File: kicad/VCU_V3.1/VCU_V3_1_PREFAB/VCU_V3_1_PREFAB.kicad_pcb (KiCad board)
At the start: 2 copper layers, 114 x 95 mm, 145 parts, among them J1 AVR-ISP-6, J2 Conn_01x24, J3 Conn_01x24, J4 Conn_01x04_Pin, J5 USB_C_Receptacle_USB2.0_14P, Q1 MMBT3906, Q2 Q_NMOS_GDS, Q3 MMBT3906, Q4 Q_NMOS_GDS, Q5 MMBT3906, Q6 Q_NMOS_GDS, Q7 MMBT3906, Q8 Q_NMOS_GDS, SW1 SW_Push, U1 ATmega328P-A, U10 TJA1051T, U11 ADuM1201AR, U12 MCP2515-xST, U13 MCP2515-xST, U14 MCP2515-xST, U16 LTV-817S, U17 ADuM1201AR, U18 ADuM1201AR, U19 OP07, U2 LM2575-5.0BU, U20 OP07, U21 OP07, U22 OP07, U23 LTV-817S, U24 LTV-817S, U25 LTV-817S, U3 CH340N, U5 TJA1051T, U6 AMS1117-3.3, U9 TJA1051T, Y1 16MHz, Y2 20MHz, Y3 20MHz, Y4 20MHz

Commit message: VCU v3.1 changes
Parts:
- removed ? (x4): , 
- added JP1: Jumper_2_Open, Jumper:SolderJumper-2_P1.3mm_Open_Pad1.0x1.5mm, F.Cu at (214.0, 75.3)
- C34, C35, C36, C37, R40, R5: moved to F.Cu
- Q2, Q4, Q6, Q8: footprint Better_Handsolder:TO-252-2 -> RMC_TO:TO-252-2
- R33: value 1k -> 500R
- R43, R44, R45, R46: moved to B.Cu
- U10, U11, U17, U18, U5, U9: footprint Package_SO:SOIC-8_3.9x4.9mm_P1.27mm -> RMC_SO:SOIC-8_3.9x4.9mm_P1.27mm_RMC_Handsolder
- U12, U13, U14: footprint Package_SO:TSSOP-20_4.4x6.5mm_P0.65mm -> RMC_SO:TSSOP-20_4.4x6.5mm_P0.65mm
- U19, U20, U21, U22: footprint Package_SO:SOIC-8-1EP_3.9x4.9mm_P1.27mm_EP2.29x3mm -> RMC_SO:SOIC-8_3.9x4.9mm_P1.27mm_RMC_Handsolder
- U3: footprint Package_SO:SOP-8_3.9x4.9mm_P1.27mm -> RMC_SO:SOIC-8_3.9x4.9mm_P1.27mm_RMC_Handsolder
- U6: footprint Package_TO_SOT_SMD:SOT-223-3_TabPin2 -> RMC_SOT:SOT-223-3_TabPin2_Handsolder
- moved C19 19.7 mm to (205.7, 114.3)
- moved R41 14.0 mm to (113.8, 111.0), turned to 180 degrees
- moved C36 7.88 mm to (153.8, 111.6), turned to -90 degrees
- moved C35 7.07 mm to (170.4, 116.8)
- moved R44 6.66 mm to (108.5, 117.3), turned to 180 degrees
- moved C34 6.24 mm to (170.4, 111.8), turned to -90 degrees
- moved R15 5.27 mm to (184.1, 127.0), turned to 180 degrees
- moved R45 5.01 mm to (108.7, 114.0), turned to 180 degrees
- moved R40 3.76 mm to (113.8, 108.8), turned to 0 degrees
- moved C37 3.28 mm to (153.8, 117.2)
- moved U5 3.07 mm to (184.1, 119.3)
- moved U9 3.04 mm to (166.2, 119.3)
- moved U10 2.75 mm to (149.9, 119.3)
- moved D2 2.15 mm to (109.9, 96.0)
- moved C20 2.11 mm to (112.9, 101.7)
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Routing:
- net +5V: track 552.8 -> 413.0 mm, vias 21 -> 20
- net CAN3-: track 125.0 -> 9.10 mm
- net CAN3+: track 123.5 -> 9.16 mm
- net CAN+: track 102.2 -> 9.16 mm
- net CAN-: track 98.3 -> 9.10 mm
- net CAN2+: track 92.6 -> 8.29 mm
- net CAN2-: track 85.8 -> 9.10 mm
- net +12V: track 176.5 -> 212.4 mm
- net APPS_3V3_GAINED: track 79.5 -> 92.6 mm
- net APPS_5V: track 112.9 -> 99.8 mm
- net Net-(R40-Pad1): track 9.45 -> 2.31 mm, vias 1 -> 0
- net +3V3: track 45.5 -> 38.4 mm
- net INPUT_BRAKE_IN: track 23.8 -> 30.7 mm
- net Net-(U11-VIA): track 6.74 -> 0.00 mm, vias 1 -> 0
- net RXD: track 87.9 -> 94.5 mm
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
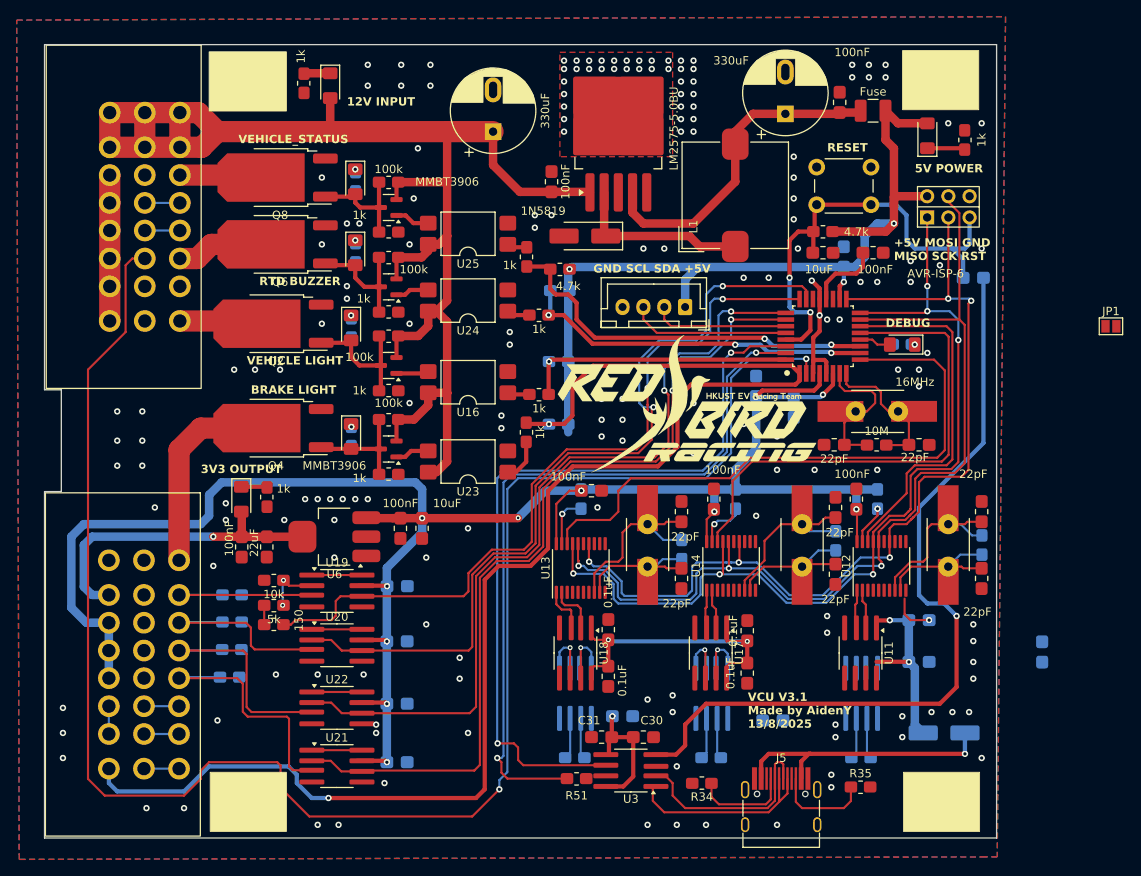
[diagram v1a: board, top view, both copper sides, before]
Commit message: VCU V3.1 preview patch v2
DRC debug
Change to pmos
remove usb c and add xh
remap pinout
rewiring
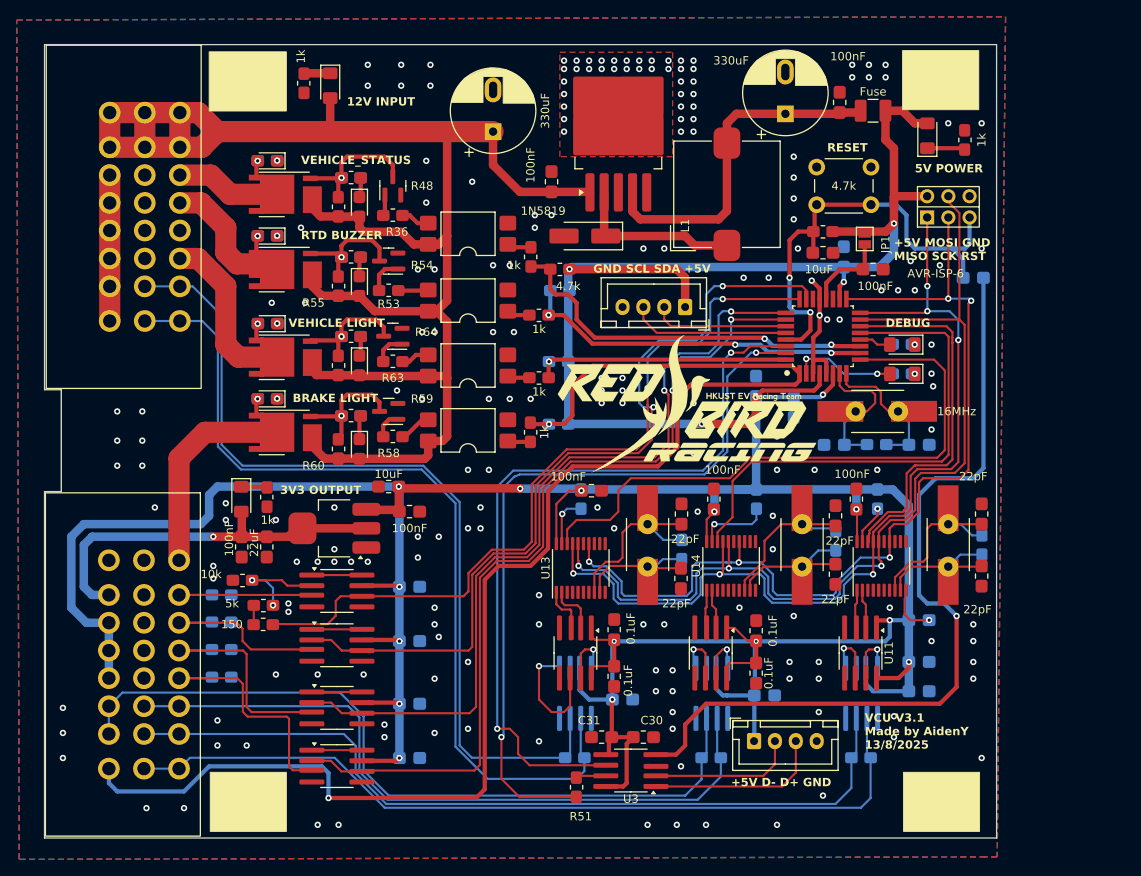
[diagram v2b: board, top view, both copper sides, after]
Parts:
- removed D4, D5, D6, D9: IR204A, LED_SMD:LED_1206_3216Metric_Pad1.42x1.75mm_HandSolder
- removed D7: D, Diode_SMD:D_SMA_Handsoldering
- removed J5: USB_C_Receptacle_USB2.0_14P, RMC_Connnector:USB_C_Receptacle_G-Switch_GT-USB-7010ASV_Handsolder
- removed Q1, Q3, Q5, Q7: MMBT3906, Package_TO_SOT_SMD:SOT-23
- removed Q2, Q4, Q6, Q8: Q_NMOS_GDS, RMC_TO:TO-252-2
- removed R12, R14, R17, R21, R25, R27: 1k, RMC_Resistor:R_0805_2012Metric_Pad1.20x1.40mm_HandSolder_L
- removed R13, R20, R26: 100k, RMC_Resistor:R_0805_2012Metric_Pad1.20x1.40mm_HandSolder_L
- removed R34: 5K1, RMC_Resistor:R_0805_2012Metric_Pad1.20x1.40mm_HandSolder_L
- removed R35: 5k1, RMC_Resistor:R_0805_2012Metric_Pad1.20x1.40mm_HandSolder_L
- added D11: IR204A, LED_SMD:LED_1206_3216Metric_Pad1.42x1.75mm_HandSolder, F.Cu at (189.0, 81.0)
- added D13: LED, RMC_LED:LED_0805_2012Metric_Pad1.45x1.40mm_HandSolder, F.Cu at (124.0, 61.0)
- added D14: LED, RMC_LED:LED_0805_2012Metric_Pad1.45x1.40mm_HandSolder, F.Cu at (113.0, 55.5)
- added D15: LED, RMC_LED:LED_0805_2012Metric_Pad1.45x1.40mm_HandSolder, F.Cu at (124.0, 70.5)
- added D16: LED, RMC_LED:LED_0805_2012Metric_Pad1.45x1.40mm_HandSolder, F.Cu at (113.0, 64.5)
- added D17: LED, RMC_LED:LED_0805_2012Metric_Pad1.45x1.40mm_HandSolder, F.Cu at (124.0, 90.0)
- added D18: LED, RMC_LED:LED_0805_2012Metric_Pad1.45x1.40mm_HandSolder, F.Cu at (113.0, 84.0)
- added D19: LED, RMC_LED:LED_0805_2012Metric_Pad1.45x1.40mm_HandSolder, F.Cu at (124.0, 80.0)
- added D20: LED, RMC_LED:LED_0805_2012Metric_Pad1.45x1.40mm_HandSolder, F.Cu at (113.0, 75.0)
- added J6: Conn_01x04_Pin, Connector_JST:JST_XH_B4B-XH-A_1x04_P2.50mm_Vertical, F.Cu at (171.2, 125.0)
- added Q11: MMBT3904, RMC_SOT:SOT-23, F.Cu at (128.0, 58.5)
- added Q12: BSC030P03NS3, RMC_SO:Infineon_PG-TDSON-8_6.15x5.15mm, F.Cu at (115.0, 59.5)
- added Q13: MMBT3904, RMC_SOT:SOT-23, F.Cu at (127.5, 67.5)
- added Q14: BSC030P03NS3, RMC_SO:Infineon_PG-TDSON-8_6.15x5.15mm, F.Cu at (115.0, 68.5)
- added Q15: MMBT3904, RMC_SOT:SOT-23, F.Cu at (127.5, 85.5)
- added Q16: BSC030P03NS3, RMC_SO:Infineon_PG-TDSON-8_6.15x5.15mm, F.Cu at (115.0, 88.0)
- added Q17: MMBT3904, RMC_SOT:SOT-23, F.Cu at (128.0, 76.5)
- added Q18: BSC030P03NS3, RMC_SO:Infineon_PG-TDSON-8_6.15x5.15mm, F.Cu at (115.0, 79.0)
- added R36: 1k, RMC_Resistor:R_0805_2012Metric_Pad1.20x1.40mm_HandSolder_L, F.Cu at (128.0, 62.0)
- added R52: 1k, RMC_Resistor:R_0805_2012Metric_Pad1.20x1.40mm_HandSolder_L, B.Cu at (113.0, 55.5)
- added R53: 1k, RMC_Resistor:R_0805_2012Metric_Pad1.20x1.40mm_HandSolder_L, F.Cu at (127.5, 71.0)
- added R54: 1k, RMC_Resistor:R_0805_2012Metric_Pad1.20x1.40mm_HandSolder_L, F.Cu at (123.0, 67.0)
- added R55: 1k, RMC_Resistor:R_0805_2012Metric_Pad1.20x1.40mm_HandSolder_L, F.Cu at (121.5, 70.5)
- added R56: 100k, RMC_Resistor:R_0805_2012Metric_Pad1.20x1.40mm_HandSolder_L, B.Cu at (123.0, 67.0)
- added R57: 1k, RMC_Resistor:R_0805_2012Metric_Pad1.20x1.40mm_HandSolder_L, B.Cu at (113.0, 64.5)
- added R58: 1k, RMC_Resistor:R_0805_2012Metric_Pad1.20x1.40mm_HandSolder_L, F.Cu at (128.0, 88.5)
- added R59: 1k, RMC_Resistor:R_0805_2012Metric_Pad1.20x1.40mm_HandSolder_L, F.Cu at (123.0, 86.0)
- added R60: 1k, RMC_Resistor:R_0805_2012Metric_Pad1.20x1.40mm_HandSolder_L, F.Cu at (121.5, 90.0)
- added R61: 100k, RMC_Resistor:R_0805_2012Metric_Pad1.20x1.40mm_HandSolder_L, B.Cu at (123.0, 86.0)
- added R62: 1k, RMC_Resistor:R_0805_2012Metric_Pad1.20x1.40mm_HandSolder_L, B.Cu at (113.0, 84.0)
- added R63: 1k, RMC_Resistor:R_0805_2012Metric_Pad1.20x1.40mm_HandSolder_L, F.Cu at (128.0, 79.5)
- added R64: 1k, RMC_Resistor:R_0805_2012Metric_Pad1.20x1.40mm_HandSolder_L, F.Cu at (123.0, 76.5)
- added R65: 1k, RMC_Resistor:R_0805_2012Metric_Pad1.20x1.40mm_HandSolder_L, F.Cu at (121.5, 80.0)
- added R66: 100k, RMC_Resistor:R_0805_2012Metric_Pad1.20x1.40mm_HandSolder_L, B.Cu at (123.0, 76.5)
- added R67: 1k, RMC_Resistor:R_0805_2012Metric_Pad1.20x1.40mm_HandSolder_L, B.Cu at (113.0, 75.0)
- added R68: 500R, RMC_Resistor:R_0805_2012Metric_Pad1.20x1.40mm_HandSolder_L, B.Cu at (189.0, 81.0)
- C10, C11, R5: moved to B.Cu
- R48: moved to F.Cu
- R49: value 100k -> 1k
- R50: value 1k -> 100k; moved to B.Cu
- moved JP1 31.3 mm to (184.5, 64.8), turned to -90 degrees
- moved C19 15.5 mm to (191.0, 119.0), turned to 0 degrees
- moved R50 7.91 mm to (123.0, 57.5), turned to 0 degrees
- moved R49 6.67 mm to (121.5, 61.0), turned to 90 degrees
- moved C18 6.40 mm to (127.5, 94.5), turned to 180 degrees
- moved R42 3.75 mm to (110.0, 105.8)
- moved U23 3.73 mm to (137.0, 87.8)
- moved C28 3.16 mm to (172.5, 119.5)
- moved R22 2.50 mm to (171.5, 96.0)
- moved C17 2.28 mm to (130.0, 97.5), turned to 0 degrees
- moved C2 2.00 mm to (185.5, 68.5)
- moved C29 2.00 mm to (155.5, 120.0)
- moved R10 2.00 mm to (145.5, 81.5)
- moved U16 2.00 mm to (137.0, 80.0)
- moved C40 1.58 mm to (130.0, 127.0)
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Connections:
- J3 pad 12: CAN3+ -> GND
- J3 pad 13: CAN3- -> GND
- J3 pad 14: PD4 -> GND
- J3 pad 15: unconnected-(J3-Pin_15-Pad15) -> CAN3+
- J3 pad 16: unconnected-(J3-Pin_16-Pad16) -> CAN3-
- J3 pad 4: CAN3+ -> BUZZER_OUT
- J3 pad 5: CAN3- -> unconnected-(J3-Pin_5-Pad5)
- J3 pad 6: BUZZER_OUT -> LED_OUTPUT
- J3 pad 7: GND -> CAN3+
- J3 pad 8: LED_OUTPUT -> CAN3-
- R48 pad 1: GND -> Net-(D13-K)
- R48 pad 2: Net-(D9-K) -> Net-(Q11-C)
- R49 pad 1: Net-(D9-A) -> +12V
- R49 pad 2: +12V -> Net-(Q11-C)
- R50 pad 1: GND -> Net-(Q11-C)
- R50 pad 2: Net-(D9-A) -> GND
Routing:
- net PD4: track 209.5 -> 12.5 mm
- net +5V: track 413.0 -> 529.6 mm
- net CAN3-: track 9.10 -> 107.0 mm
- net CAN3+: track 9.16 -> 104.8 mm
- net CAN-: track 9.10 -> 100.2 mm
- net CAN+: track 9.16 -> 99.5 mm
- net CAN2+: track 8.29 -> 92.2 mm
- net CAN2-: track 9.10 -> 85.8 mm
- net Net-(D7-A): track 32.9 -> 0.00 mm, vias 1 -> 0
- net +12V: track 212.4 -> 239.1 mm
- net Net-(D4-A): track 16.4 -> 0.00 mm
- net Net-(Q11-C): track 0.00 -> 16.4 mm, vias 0 -> 1
- net Net-(D6-A): track 15.4 -> 0.00 mm
- net Net-(Q15-C): track 0.00 -> 14.9 mm, vias 0 -> 1
- net Net-(Q17-C): track 0.00 -> 14.6 mm, vias 0 -> 1
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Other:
- board text added: "+5V D- D+ GND"

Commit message: L
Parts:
- C27: moved to B.Cu
- moved C27 3.45 mm to (148.5, 96.0), turned to 90 degrees
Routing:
- net Net-(U10-TXD): track 14.6 -> 6.42 mm
- net D-: track 19.1 -> 21.6 mm
- net +5V: track 529.6 -> 528.1 mm
- net RST: track 55.2 -> 54.6 mm
- net CS3: track 72.6 -> 73.2 mm
- net GND: vias 198 -> 240
